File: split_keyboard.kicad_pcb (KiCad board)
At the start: 2 copper layers, 307.5 x 126.2 mm, 224 parts

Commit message: Added images and logo
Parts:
- added G***: LOGO, custom:DHC_Logo, B.Cu at (172.2, 102.2)
- added kibuzzard-6602E1CF: G***, kibuzzard-6602E1CF, B.Cu at (208.0, 103.2)
- added kibuzzard-6603142B: G***, kibuzzard-6603142B, F.Cu at (322.6, 27.2)
- added kibuzzard-6603143E: G***, kibuzzard-6603143E, F.Cu at (54.2, 27.1)
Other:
- board text removed: "Split Keyboard v0.2 --- Left Side"
- board text removed: "Split Keyboard v0.2 --- Right Side"

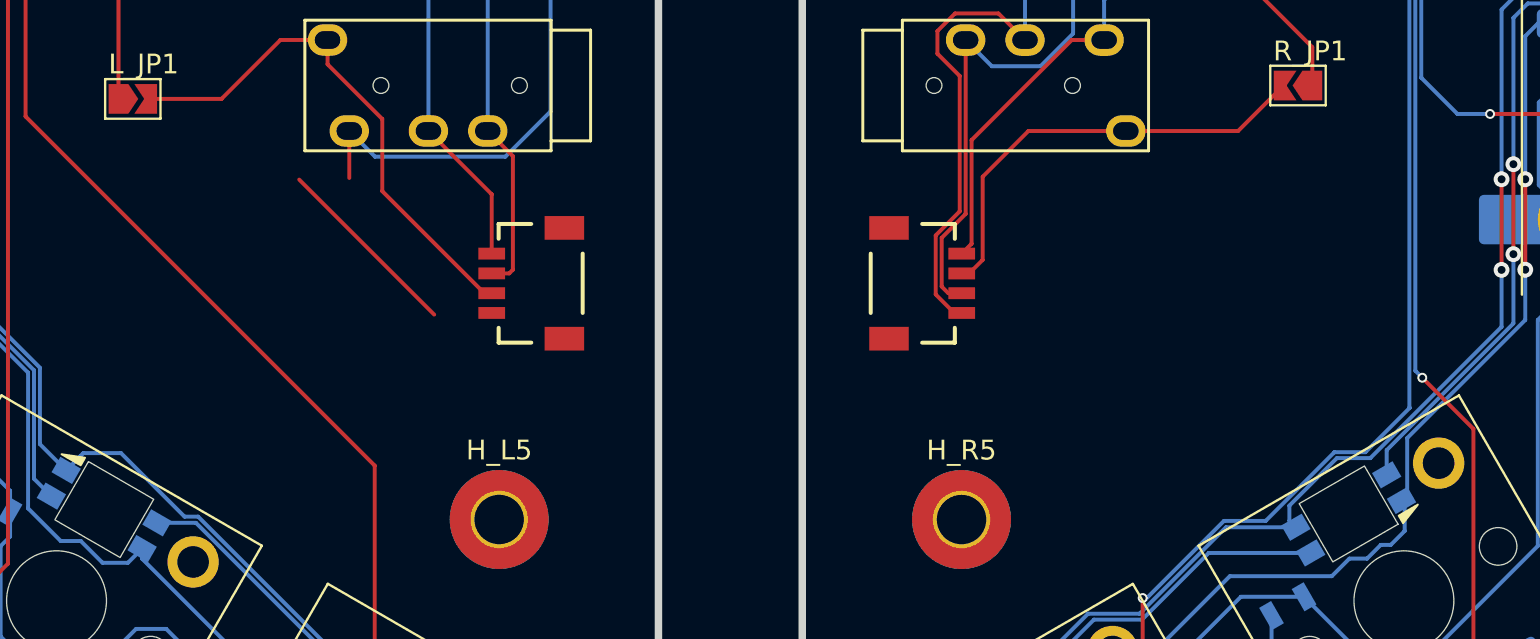
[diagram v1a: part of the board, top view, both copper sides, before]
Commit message: Added images to silkscreen
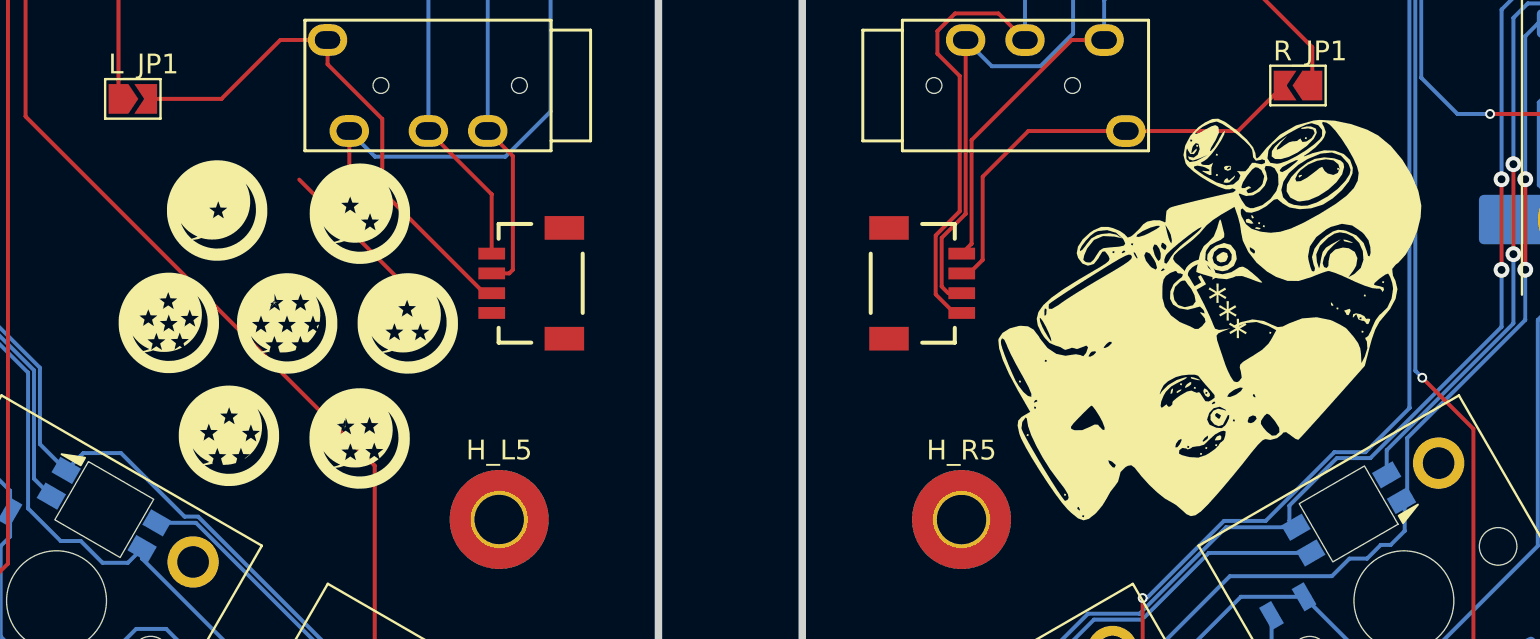
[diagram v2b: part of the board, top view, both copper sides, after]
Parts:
- added G***: LOGO, custom:Toriyama-Chibi, F.Cu at (212.1, 103.0)
- added G***: LOGO, custom:Dragon-Ball, F.Cu at (162.8, 107.4)
